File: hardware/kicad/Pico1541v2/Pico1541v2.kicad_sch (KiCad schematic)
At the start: 53 parts, among them J1 SWD, J2 Serial, J3 Display/Keys, J4 Micro SD Card, J5 5V_EXT, J6 USB_A, J7 OLED/Key_Hat, J8 OLED, J9 DIN-6, Q1 MMBT3904, SW1 Reset, SW2 Button1, SW3 Button3, SW4 Button2, SW5 Button4, U1 74LS05, U2 SRV05-4

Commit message: More work on v2 hardware version.
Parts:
- removed C3, C6: 47u, Capacitor_SMD:CP_Elec_5x5.4, symbol Device:C_Polarized
- removed C5: 100n, Capacitor_SMD:C_0603_1608Metric_Pad1.08x0.95mm_HandSolder, symbol Device:C
- removed D1: SS14, Diode_SMD:D_SMA, symbol Diode:SS14
- removed J5: 5V_EXT, Connector_BarrelJack:BarrelJack_CUI_PJ-063AH_Horizontal_CircularHoles, symbol Connector:Barrel_Jack_MountingPin
- removed J6: USB_A, Connector_USB:USB_A_Connfly_DS1095, symbol Connector:USB_A
- removed JP1: EXT_5V, Jumper:SolderJumper-2_P1.3mm_Bridged_RoundedPad1.0x1.5mm, symbol Jumper:Jumper_2_Bridged
- added C3: 10u, Capacitor_SMD:C_0603_1608Metric_Pad1.08x0.95mm_HandSolder, symbol Device:C
- added R4: 1k, Resistor_SMD:R_0603_1608Metric_Pad0.98x0.95mm_HandSolder, symbol Device:R
- C1: footprint Capacitor_SMD:CP_Elec_5x5.4 -> Capacitor_SMD:CP_Elec_5x4.5
- D1: renamed from D2; footprint Pico1541-footprints:LED_D5.0mm-4_RGB_CorrectStaggered_Pins -> Pico1541 Footprints:LED_D5.0mm-4_RGB_CorrectStaggered_Pins
- J4: footprint Pico1541-footprints:MicroSD_HPJF -> Pico1541 Footprints:MicroSD_HPJF
- J7: renamed from J9; footprint Pico1541-footprints:DIN-6-240deg -> Pico1541 Footprints:DIN-6-240deg
- RN3, RN4: value 4k7 -> 1k
- SW3: value Button3 -> Button2
- SW4: renamed from SW5; value Button4 -> Button3
- SW5: renamed from SW4; value Button2 -> Button4
- renumbered C7 to C5, D3 to D2, J7 to J5, J8 to J6, R2 to R1, R1 to R2
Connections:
- net VBUS is gone; now on net +5V: A1.40 (VBUS)
- net +3.3V: now also C3.1; no longer C1.1
- net +5V: now also C1.1, R4.1
- net GND: now also C3.2, R4.2; no longer A1.TP1 (USB_GND)
- net GNDA: now also SW2.2, SW3.2, SW4.2, SW5.2
- net at J5.7 (Pin_7), SW4.1: no longer SW5.1
- net USB_DN: no longer names the net of A1.TP2 (USB_DM)
- net USB_DP: no longer names the net of A1.TP3 (USB_DP)
- net VS: no longer names the net of A1.39 (VSYS)
- new net: J5.6 (Pin_6), SW3.1
- new net: J5.8 (Pin_8), SW5.1
- new net: J5.5 (Pin_5), SW2.1
- no-connect marks 9 -> 14
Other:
- note removed: "For external power, cut JP1 and install D3."
- moved on the sheet: C2, C4, FID1, FID2, FID3, H1, H2, H3, H4, H5, H6, J4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

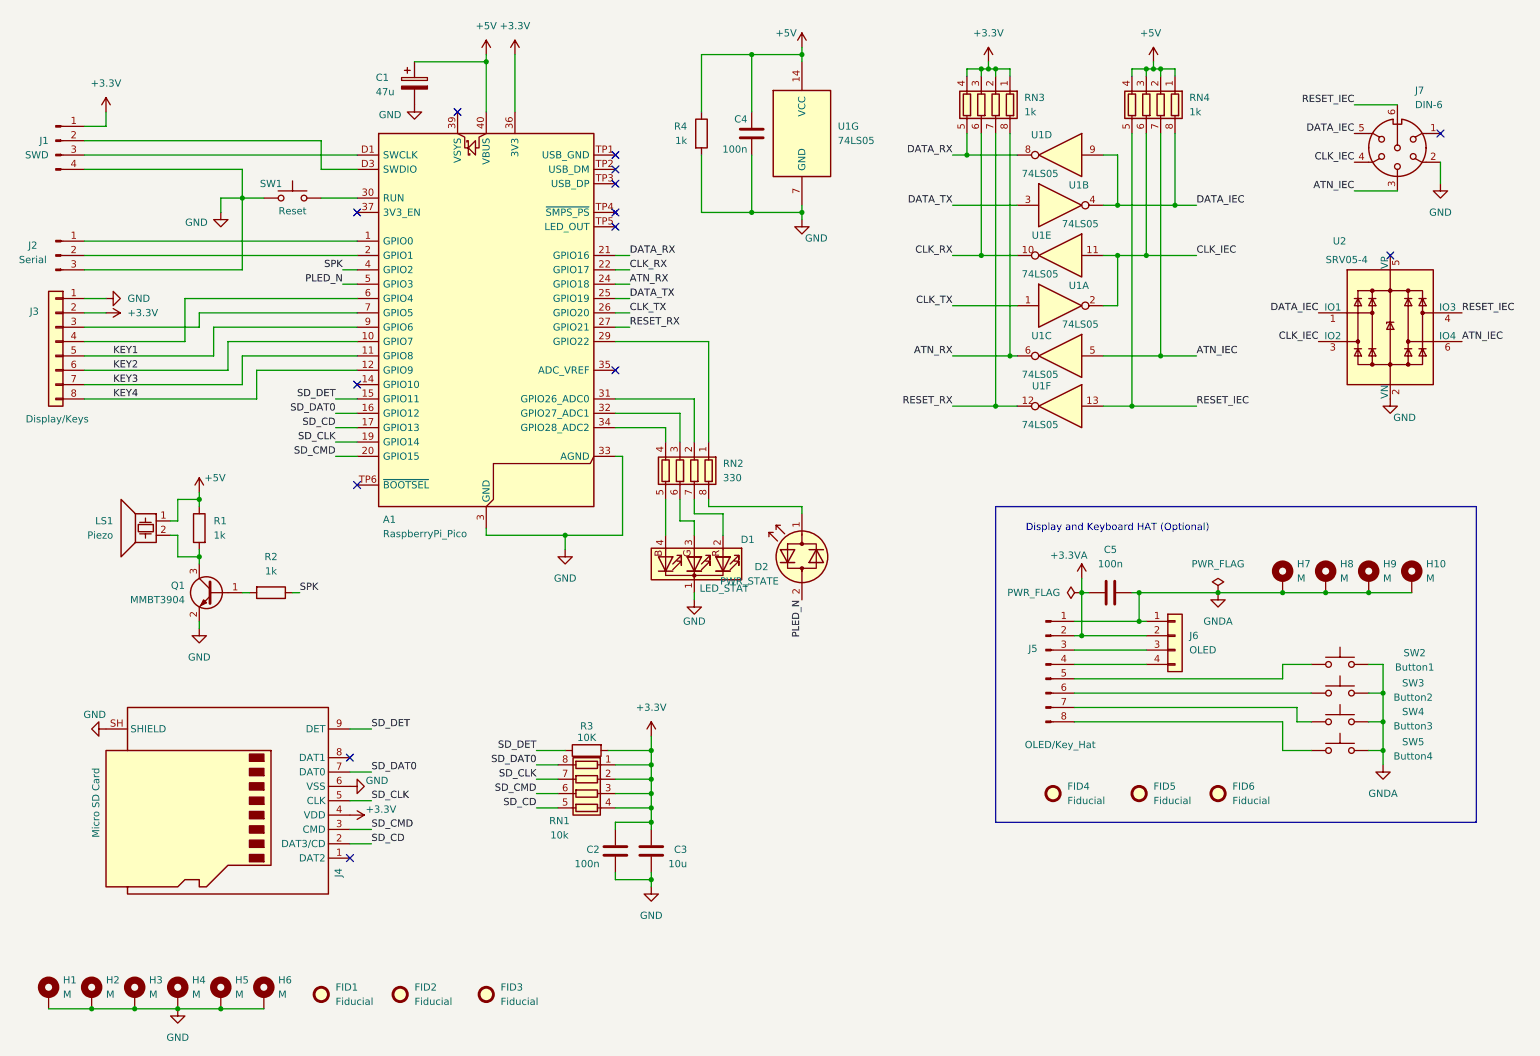
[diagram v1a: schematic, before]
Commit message: Reduced the ATN poll interval to 4. This did not improve ATN driven demo loader sadly.
Updated v2 schematic.
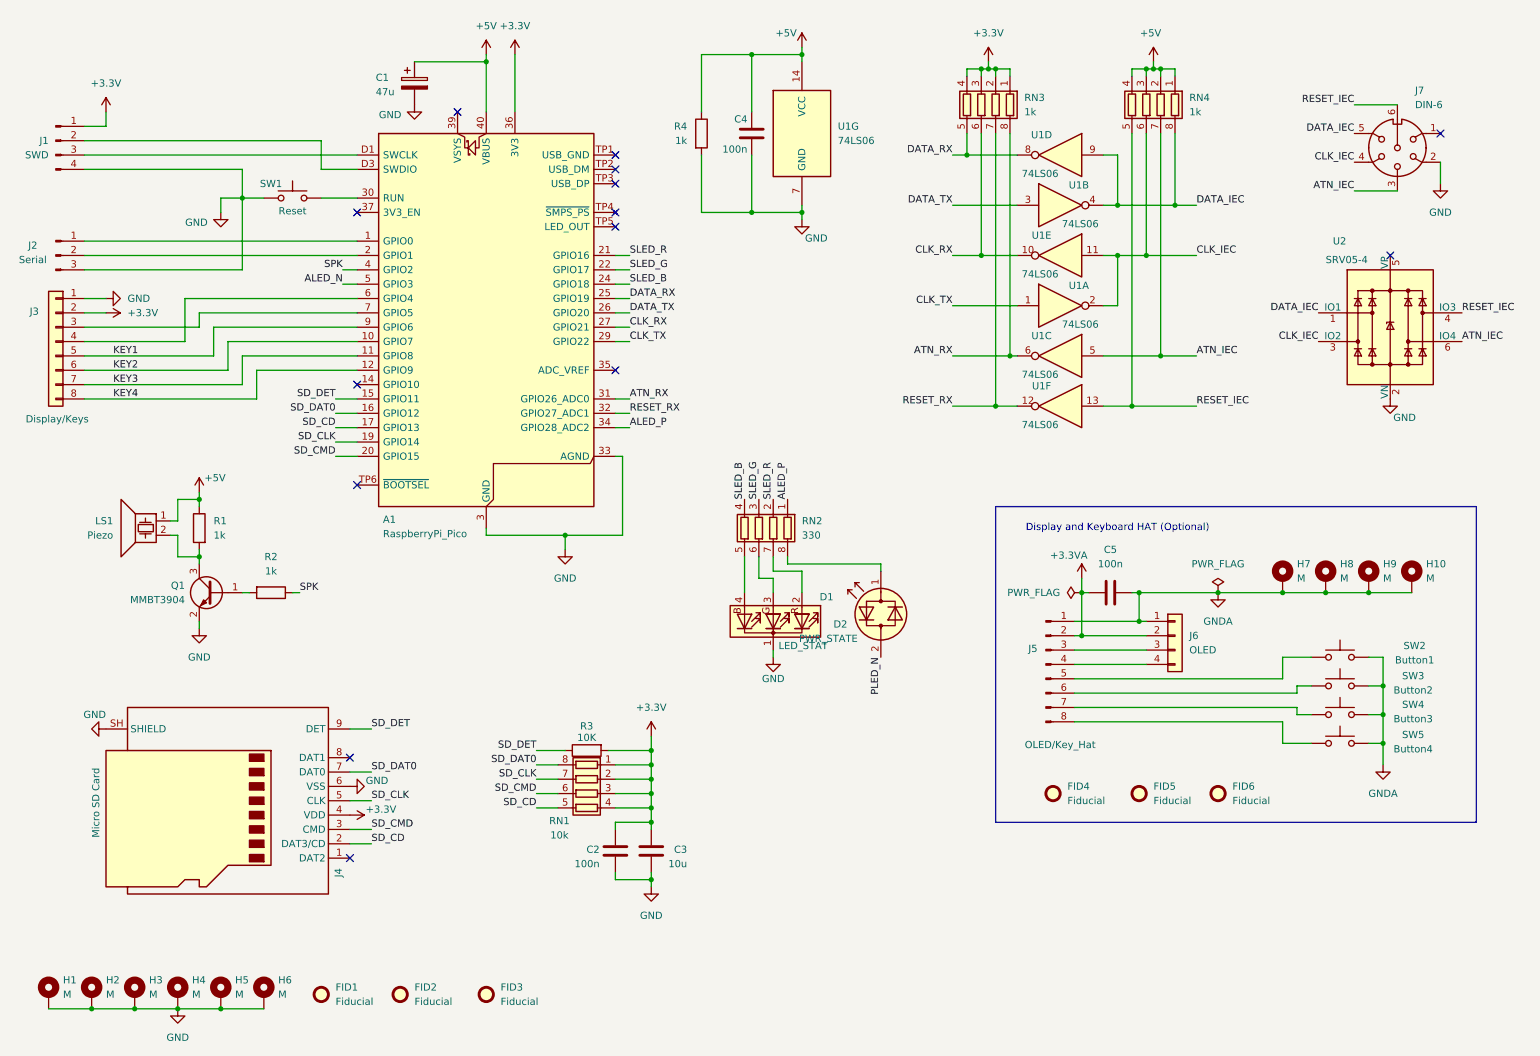
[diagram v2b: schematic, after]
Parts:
- U1: value 74LS05 -> 74LS06
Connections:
- net ATN_RX: now also A1.31 (GPIO26_ADC0); no longer A1.24 (GPIO18)
- net CLK_RX: now also A1.27 (GPIO21); no longer A1.22 (GPIO17)
- net CLK_TX: now also A1.29 (GPIO22); no longer A1.26 (GPIO20)
- net DATA_RX: now also A1.25 (GPIO19); no longer A1.21 (GPIO16)
- net DATA_TX: now also A1.26 (GPIO20); no longer A1.25 (GPIO19)
- net PLED_N: no longer A1.5 (GPIO3)
- net RESET_RX: now also A1.32 (GPIO27_ADC1); no longer A1.27 (GPIO21)
- net ALED_P: now reaches RN2.1 (R1.1)
- net ALED_P: now also A1.34 (GPIO28_ADC2); no longer A1.29 (GPIO22)
- net SLED_R: now reaches RN2.2 (R2.1)
- net SLED_R: now also A1.21 (GPIO16); no longer A1.31 (GPIO26_ADC0)
- net SLED_G: now reaches RN2.3 (R3.1)
- net SLED_G: now also A1.22 (GPIO17); no longer A1.32 (GPIO27_ADC1)
- net SLED_B: now reaches RN2.4 (R4.1)
- net SLED_B: now also A1.24 (GPIO18); no longer A1.34 (GPIO28_ADC2)
- new net ALED_N: A1.5 (GPIO3)
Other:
- moved on the sheet: D1, D2, RN2, SW2, SW3, SW4, SW5
